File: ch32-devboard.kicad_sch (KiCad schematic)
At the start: 8 parts, among them J1 USB_C_Receptacle_USB2.0_16P, J2 Conn_01x10_Pin, J3 Conn_01x10_Pin, J4 Conn_01x03_Socket, J5 Conn_01x05_Pin

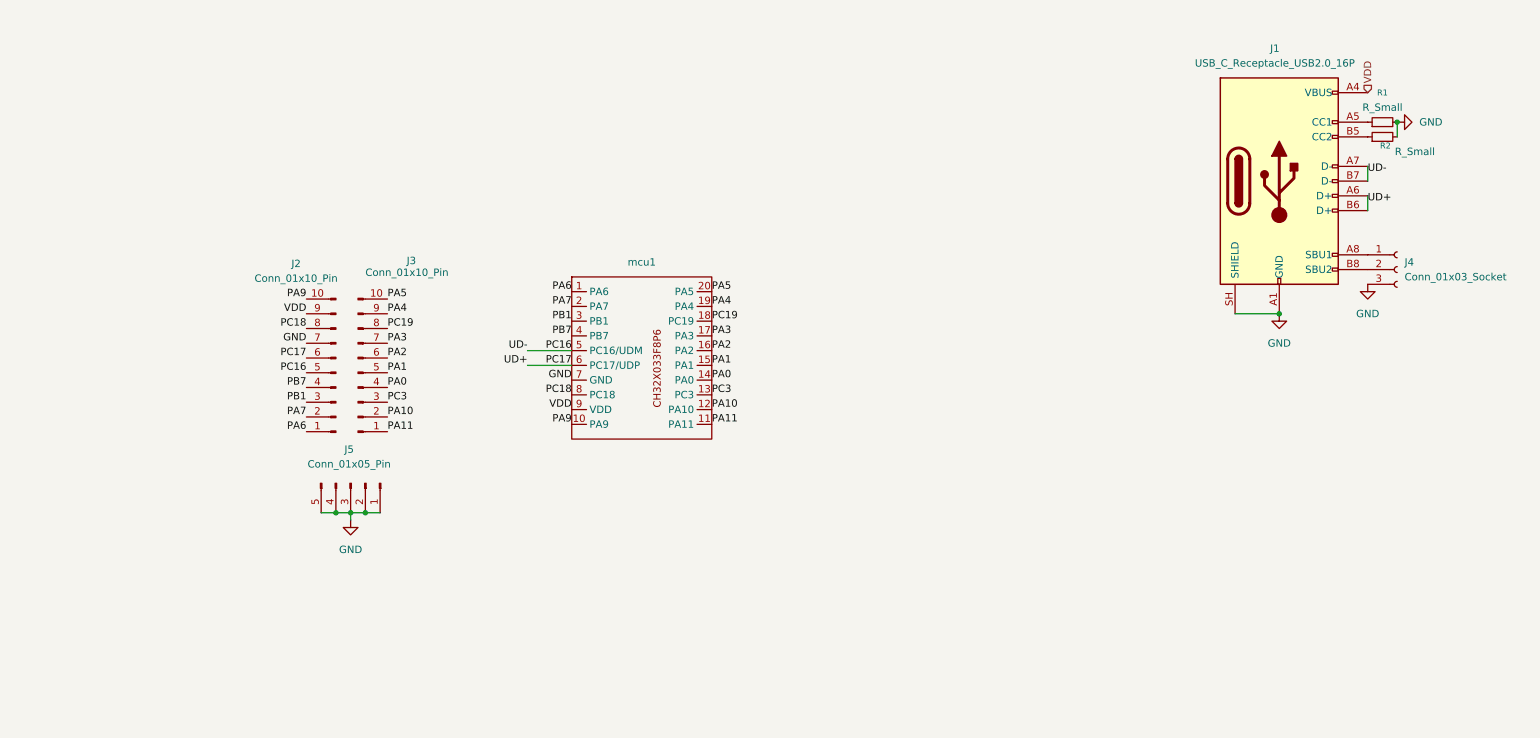
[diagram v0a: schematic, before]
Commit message: add leds,decouple vdd, resistory for d+ d-
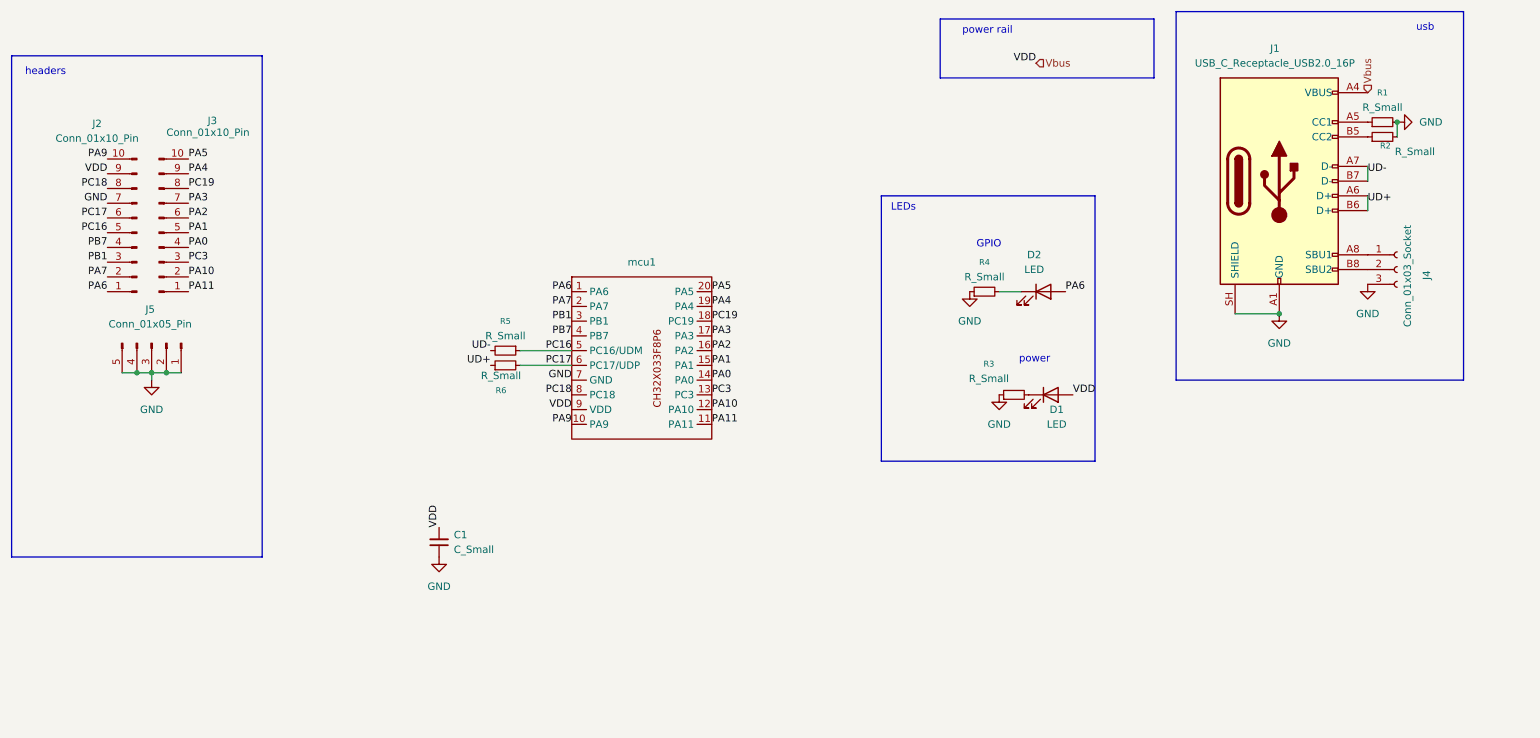
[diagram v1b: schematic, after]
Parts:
- added C1: C_Small, Capacitor_SMD:C_0805_2012Metric_Pad1.18x1.45mm_HandSolder, symbol Device:C_Small
- added D1, D2: LED, LED_SMD:LED_0805_2012Metric_Pad1.15x1.40mm_HandSolder, symbol Device:LED
- added R3, R4, R5, R6: R_Small, Resistor_SMD:R_0805_2012Metric_Pad1.20x1.40mm_HandSolder, symbol Device:R_Small
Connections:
- net GND: now also C1.1, R3.1, R4.1
- net PA6: now also D2.2 (A)
- net PC16: now also R5.1; no longer J1.A7 (D-), J1.B7 (D-)
- net PC17: now also R6.2; no longer J1.A6 (D+), J1.B6 (D+)
- net VDD renamed Vbus
- net Vbus: now also C1.2, D1.2 (A)
- new net: D1.1 (K), R3.2
- new net: D2.1 (K), R4.2
- new net UD+: J1.A6 (D+), J1.B6 (D+), R6.1
- new net UD-: J1.A7 (D-), J1.B7 (D-), R5.2
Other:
- note added: "GPIO"
- note added: "LEDs"
- note added: "headers"
- note added: "power"
- note added: "power rail"
- note added: "usb"
- moved on the sheet: J2, J3, J5

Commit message: complete with ch32x033
no proper button footprint
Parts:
- added R7: R, Resistor_SMD:R_0805_2012Metric_Pad1.20x1.40mm_HandSolder, symbol Device:R
- added SW1: CK_KMS2xxG, Button_Switch_SMD:SW_SPST_CK_KMS2xxGP, symbol Switch:CK_KMS2xxG
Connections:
- net GND: now also R7.2, SW1.SH (B)
- net Vbus: now also SW1.2
- new net: R7.1, SW1.1

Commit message: add ldo, change button footprint, reroute and compact, label pins
give value to resistors and capacitors, remove series resistor from usb line, correct reset button pullup resistor from pulldown
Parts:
- removed R5, R6: R_Small, Resistor_SMD:R_0805_2012Metric_Pad1.20x1.40mm_HandSolder, symbol Device:R_Small
- added C1: 0.1uF, Capacitor_SMD:C_0805_2012Metric_Pad1.18x1.45mm_HandSolder, symbol Device:C_Small
- added C3, C4: 4.7uF, Capacitor_SMD:C_0805_2012Metric_Pad1.18x1.45mm_HandSolder, symbol Device:C_Small
- added U1: AP2112K-3.3, Package_TO_SOT_SMD:SOT-23-5, symbol Regulator_Linear:AP2112K-3.3
- C2: renamed from C1; value C_Small -> 1uF
- R1: renamed from R7; value R -> 10k
- R2: renamed from R4; value R_Small -> 1k
- R3: value R_Small -> 1k
- R4: renamed from R1; value R_Small -> 5.1k
- R5: renamed from R2; value R_Small -> 5.1k
- SW1: footprint Button_Switch_SMD:SW_SPST_CK_KMS2xxGP -> CH32-devBoard:smd-push-button-TS3425PA
- renumbered D2 to D1, D1 to D2, J2 to J1, J5 to J2, J1 to J4, J4 to J5
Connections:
- net GND: now also SW1.2, C1.1, C3.1, C4.1, U1.2 (GND); no longer R1.2
- net PA9: now also J1.6 (Pin_6); no longer J1.10 (Pin_10)
- net PC18: now also J1.5 (Pin_5); no longer J1.8 (Pin_8)
- net UD+: now also mcu1.6 (PC17/UDP)
- net UD-: now also mcu1.5 (PC16/UDM)
- net Vbus: now also J1.10 (Pin_10), C4.2, U1.1 (VIN), U1.3 (EN); no longer C2.2, D2.2 (A), J1.9 (Pin_9), SW1.2, mcu1.9 (VDD)
- removed net PC16: J1.5 (Pin_5), mcu1.5 (PC16/UDM)
- removed net PC17: J1.6 (Pin_6), mcu1.6 (PC17/UDP)
- new net VDD: C1.2, C2.2, C3.2, D2.2 (A), J1.8 (Pin_8), J1.9 (Pin_9), R1.2, U1.5 (VOUT), mcu1.9 (VDD)
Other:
- moved on the sheet: C2, J1, J3

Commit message: add license notice in schematic file
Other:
- company: (none) -> Param foundation
- title: (none) -> ch32 devboard
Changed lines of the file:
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@@
 	(generator_version "10.0")
 	(paper "A4")
+	(title_block
+		(title "ch32 devboard")
+		(company "Param foundation")
+		(comment 1 "designed in param makers adda")
+		(comment 2 "license: CERN-OHL-W V2.0")
+		(comment 3 "dev board schematic")
+	)
 	(rectangle
 		(start 173.99 46.99)

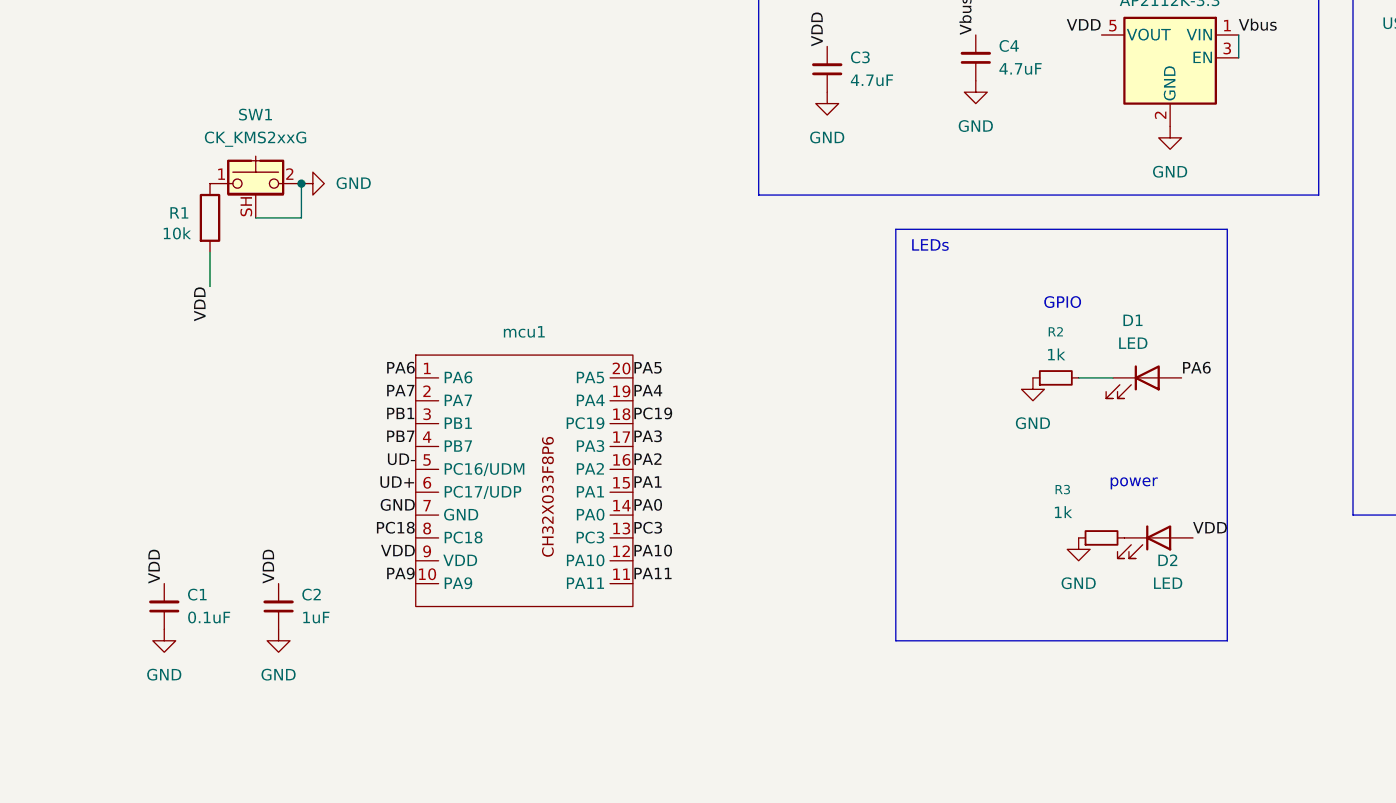
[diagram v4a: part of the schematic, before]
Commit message: connect reset button to mcu, compact reroute
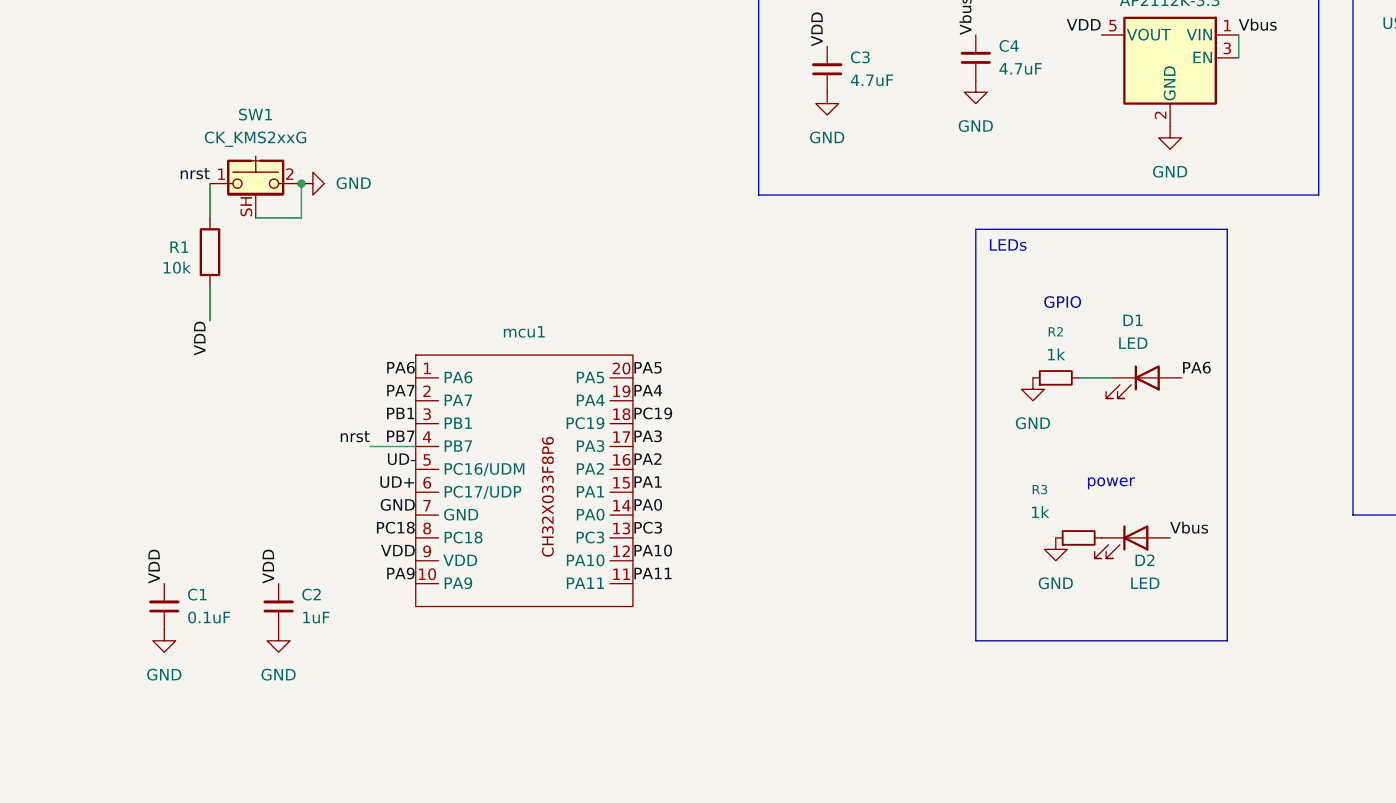
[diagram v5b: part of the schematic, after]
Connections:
- net PB7: now also R1.1, SW1.1
- net VDD: no longer D2.2 (A)
- net Vbus: now also D2.2 (A)
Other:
- moved on the sheet: D2, R1, R3
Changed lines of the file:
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@@
 	)
 	(rectangle
-		(start 173.99 46.99)
+		(start 182.88 46.99)
 		(end 210.82 92.71)
 		(stroke
@@
 	(text "power"
 		(exclude_from_sim no)
-		(at 200.406 75.184 0)
+		(at 197.866 75.184 0)
 		(effects
 			(font
@@
 	(text "LEDs"
 		(exclude_from_sim no)
-		(at 177.8 49.022 0)
+		(at 186.436 49.022 0)
 		(effects
 			(font
@@
 	(wire
 		(pts
+			(xy 97.79 45.72) (xy 97.79 41.91)
+		)
+		(stroke
+			(width 0)
+			(type default)
+		)
+	)
+	(wire
+		(pts
 			(xy 102.87 45.72) (xy 107.95 45.72)
 		)
@@
 	(wire
 		(pts
-			(xy 97.79 49.53) (xy 97.79 53.34)
+			(xy 97.79 53.34) (xy 97.79 57.15)
 		)
 		(stroke
@@
 	(wire
 		(pts
+			(xy 115.57 71.12) (xy 120.65 71.12)
+		)
+		(stroke
+			(width 0)
+			(type default)
+		)
+	)
+	(wire
+		(pts
 			(xy 257.81 41.91) (xy 257.81 44.45)
 		)
@@
 		)
 	)
+	(label "nrst"
+		(at 97.79 41.91 180)
+		(effects
+			(font
+				(size 1.27 1.27)
+			)
+			(justify right bottom)
+		)
+	)
 	(label "UD+"
 		(at 120.65 76.2 180)
@@
 		)
 	)
+	(label "nrst"
+		(at 115.57 71.12 180)
+		(effects
+			(font
+				(size 1.27 1.27)
+			)
+			(justify right bottom)
+		)
+	)
 	(label "PC19"
 		(at 144.78 68.58 0)
@@
 		)
 	)
-	(label "VDD"
-		(at 207.01 81.28 0)
+	(label "Vbus"
+		(at 204.47 81.28 0)
 		(effects
 			(font
@@
 	)
 	(label "VDD"
-		(at 97.79 53.34 270)
+		(at 97.79 57.15 270)
 		(effects
 			(font
@@
 		(dnp no)
 		(fields_autoplaced yes)
-		(property "Reference" "#PWR04"
+		(property "Reference" "#PWR03"
 			(at 105.41 97.79 0)
 			(hide yes)
@@
 			(project "ch32-devboard"
 				(path "/4100db7a-d523-4b09-b3c1-238f0387dfea"
-					(reference "#PWR04")
+					(reference "#PWR03")
 					(unit 1)
 				)
@@
 	(symbol
 		(lib_id "Device:R")
-		(at 97.79 45.72 0)
+		(at 97.79 49.53 0)
 		(unit 1)
 		(body_style 1)
@@
 		(dnp no)
 		(property "Reference" "R1"
-			(at 93.218 45.212 0)
+			(at 93.218 49.022 0)
 			(show_name no)
 			(do_not_autoplace no)
@@
 		)
 		(property "Value" "10k"
-			(at 92.456 47.498 0)
+			(at 92.456 51.308 0)
 			(show_name no)
 			(do_not_autoplace no)
@@
 		)
 		(property "Footprint" "Resistor_SMD:R_0805_2012Metric_Pad1.20x1.40mm_HandSolder"
-			(at 96.012 45.72 90)
+			(at 96.012 49.53 90)
 			(hide yes)
 			(show_name no)
@@
 		)
 		(property "Datasheet" ""
-			(at 97.79 45.72 0)
+			(at 97.79 49.53 0)
 			(hide yes)
 			(show_name no)
@@
 		)
 		(property "Description" "Resistor"
-			(at 97.79 45.72 0)
+			(at 97.79 49.53 0)
 			(hide yes)
 			(show_name no)
@@
 	(symbol
 		(lib_id "Device:R_Small")
-		(at 196.85 81.28 90)
+		(at 194.31 81.28 90)
 		(unit 1)
 		(body_style 1)
@@
 		(dnp no)
 		(property "Reference" "R3"
-			(at 192.532 75.946 90)
+			(at 189.992 75.946 90)
 			(show_name no)
 			(do_not_autoplace no)
@@
 		)
 		(property "Value" "1k"
-			(at 192.532 78.486 90)
+			(at 189.992 78.486 90)
 			(show_name no)
 			(do_not_autoplace no)
@@
 		)
 		(property "Footprint" "Resistor_SMD:R_0805_2012Metric_Pad1.20x1.40mm_HandSolder"
-			(at 196.85 81.28 0)
+			(at 194.31 81.28 0)
 			(hide yes)
 			(show_name no)
@@
 		)
 		(property "Datasheet" ""
-			(at 196.85 81.28 0)
+			(at 194.31 81.28 0)
 			(hide yes)
 			(show_name no)
@@
 		)
 		(property "Description" "Resistor, small symbol"
-			(at 196.85 81.28 0)
+			(at 194.31 81.28 0)
 			(hide yes)
 			(show_name no)
@@
 	(symbol
 		(lib_id "power:GND")
-		(at 194.31 81.28 0)
+		(at 191.77 81.28 0)
 		(unit 1)
 		(body_style 1)
@@
 		(fields_autoplaced yes)
 		(property "Reference" "#PWR08"
-			(at 194.31 87.63 0)
+			(at 191.77 87.63 0)
 			(hide yes)
 			(show_name no)
@@
 		)
 		(property "Value" "GND"
-			(at 194.31 86.36 0)
+			(at 191.77 86.36 0)
 			(show_name no)
 			(do_not_autoplace no)
@@
 		)
 		(property "Footprint" ""
-			(at 194.31 81.28 0)
+			(at 191.77 81.28 0)
 			(hide yes)
 			(show_name no)
@@
 		)
 		(property "Datasheet" ""
-			(at 194.31 81.28 0)
+			(at 191.77 81.28 0)
 			(hide yes)
 			(show_name no)
@@
 		)
 		(property "Description" "Power symbol creates a global label with name \"GND\" , ground"
-			(at 194.31 81.28 0)
+			(at 191.77 81.28 0)
 			(hide yes)
 			(show_name no)
@@
 	(symbol
 		(lib_id "Device:LED")
-		(at 203.2 81.28 0)
+		(at 200.66 81.28 0)
 		(unit 1)
 		(body_style 1)
@@
 		(dnp no)
 		(property "Reference" "D2"
-			(at 204.216 83.82 0)
+			(at 201.676 83.82 0)
 			(show_name no)
 			(do_not_autoplace no)
@@
 		)
 		(property "Value" "LED"
-			(at 204.216 86.36 0)
+			(at 201.676 86.36 0)
 			(show_name no)
 			(do_not_autoplace no)
@@
 		)
 		(property "Footprint" "LED_SMD:LED_0805_2012Metric_Pad1.15x1.40mm_HandSolder"
-			(at 203.2 81.28 0)
+			(at 200.66 81.28 0)
 			(hide yes)
 			(show_name no)
@@
 		)
 		(property "Datasheet" ""
-			(at 203.2 81.28 0)
+			(at 200.66 81.28 0)
 			(hide yes)
 			(show_name no)
@@
 		)
 		(property "Description" "Light emitting diode"
-			(at 203.2 81.28 0)
+			(at 200.66 81.28 0)
 			(hide yes)
 			(show_name no)
@@
 		)
 		(property "Sim.Pins" "1=K 2=A"
-			(at 203.2 81.28 0)
+			(at 200.66 81.28 0)
 			(hide yes)
 			(show_name no)
@@
 		(dnp no)
 		(fields_autoplaced yes)
-		(property "Reference" "#PWR03"
+		(property "Reference" "#PWR04"
 			(at 114.3 41.91 0)
 			(hide yes)
@@
 			(project "ch32-devboard"
 				(path "/4100db7a-d523-4b09-b3c1-238f0387dfea"
-					(reference "#PWR03")
+					(reference "#PWR04")
 					(unit 1)
 				)
